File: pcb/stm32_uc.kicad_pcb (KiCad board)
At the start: 2 copper layers, 28 parts, among them J1 Conn_01x18_Male, J2 Conn_01x18_Male, J3 USB_C_Receptacle_USB2.0, J4 Conn_01x04_Male, SW1 SW_SPDT, U1 AMS1117-3.3, U2 STM32F103C8T6, Y1 16Mhz

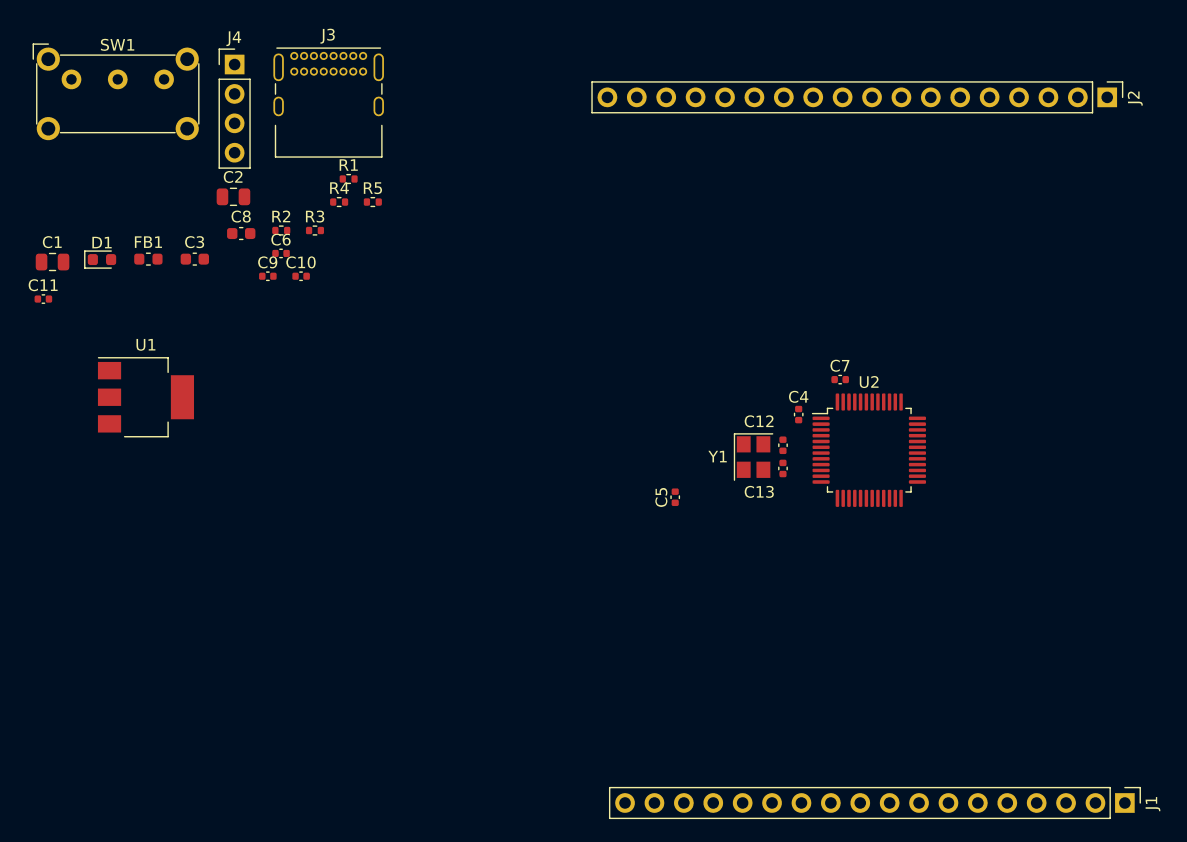
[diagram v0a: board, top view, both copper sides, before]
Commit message: fix pin header pinout
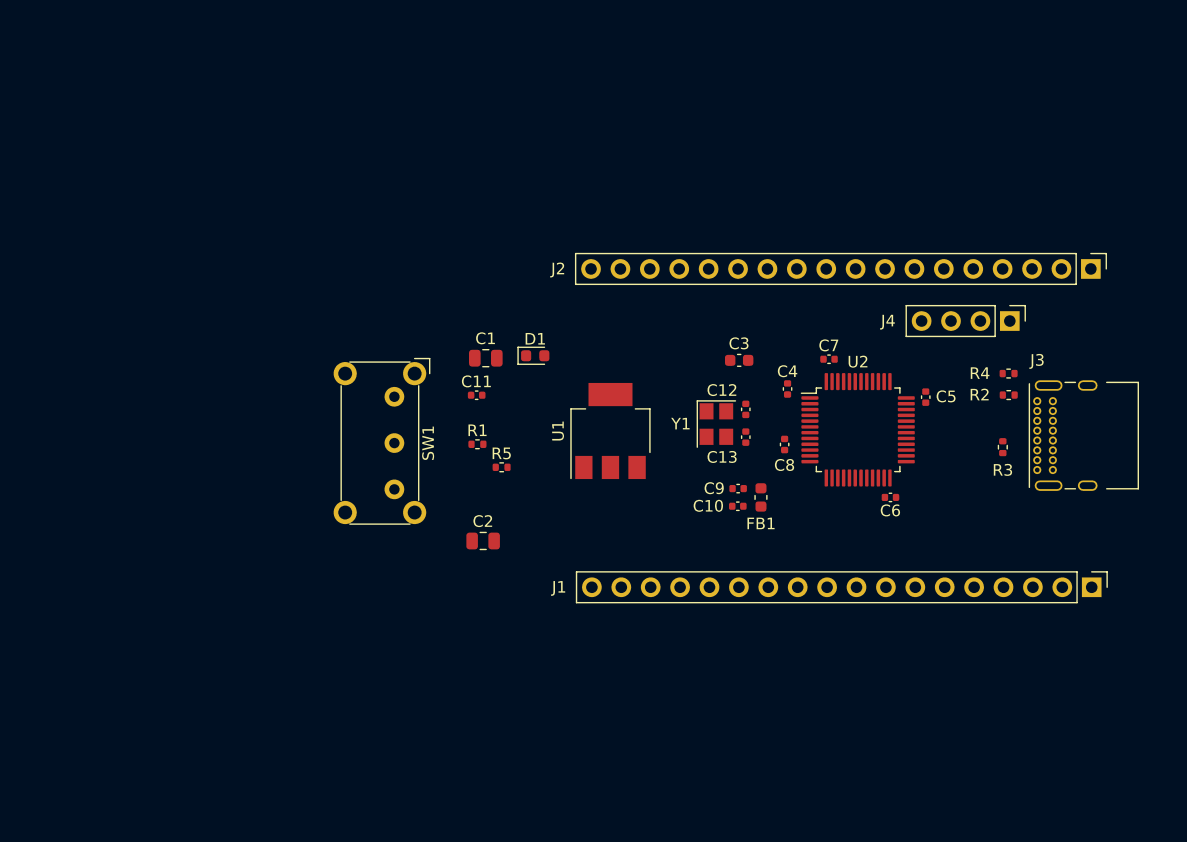
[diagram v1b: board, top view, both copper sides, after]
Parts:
- C8: footprint Capacitor_SMD:C_0603_1608Metric -> Capacitor_SMD:C_0402_1005Metric
- moved J3 73.5 mm to (195.9, 106.9), turned to 90 degrees
- moved J4 70.5 mm to (193.5, 94.0), turned to -90 degrees
- moved R2 64.4 mm to (193.4, 100.4), turned to 180 degrees
- moved R3 62.3 mm to (192.9, 104.9), turned to 90 degrees
- moved R4 59.7 mm to (193.4, 98.5), turned to 180 degrees
- moved FB1 56.8 mm to (172.0, 109.2), turned to -90 degrees
- moved C6 56.7 mm to (183.2, 109.2), turned to 180 degrees
- moved C8 50.4 mm to (174.0, 104.7), turned to 90 degrees
- moved C3 47.8 mm to (170.1, 97.4)
- moved C9 44.6 mm to (170.0, 108.5), turned to 180 degrees
- moved C10 42.6 mm to (170.0, 110.0), turned to 180 degrees
- moved U1 40.2 mm to (159.0, 103.5), turned to 90 degrees
- moved SW1 39.1 mm to (140.3, 100.5), turned to -90 degrees
- moved D1 38.3 mm to (152.5, 97.0)
- moved C11 38.3 mm to (147.4, 100.4)
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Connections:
- J1 pad 10: /PA3 -> /PA7
- J1 pad 11: /PA4 -> /PA6
- J1 pad 13: /PA6 -> /PA4
- J1 pad 14: /PA7 -> /PA3
- J1 pad 15: /PA8 -> /PA2
- J1 pad 16: /PA9 -> /PA1
- J1 pad 17: /PA15 -> /PA0
- J1 pad 2: /PB11 -> /PB14
- J1 pad 3: /PB12 -> /PB13
- J1 pad 4: /PB13 -> /PB12
- J1 pad 5: /PB14 -> /PB11
- J1 pad 6: /PB15 -> /PB10
- J1 pad 7: /PA0 -> /PB2
- J1 pad 8: /PA1 -> /PB1
- J1 pad 9: /PA2 -> /PB0
- J2 pad 10: /PB4 -> /PB7
- J2 pad 11: /PB5 -> /PB8
- J2 pad 12: /PB6 -> /PB9
- J2 pad 13: /PB7 -> unconnected-(J2-Pad13)
- J2 pad 14: /PB8 -> /PC13
- J2 pad 15: /PB9 -> /PC14
- J2 pad 16: /PB10 -> /PC15
- J2 pad 3: /PC13 -> /PB15
- J2 pad 4: /PC14 -> /PA8
- J2 pad 5: /PC15 -> /PA9
- J2 pad 6: /PB0 -> /PB3
- J2 pad 7: /PB1 -> /PB4
- J2 pad 8: /PB2 -> /PB5
- J2 pad 9: /PB3 -> /PB6
- J3 pad A6: Net-(J3-PadA6) -> /USB_D+
- J3 pad A7: Net-(J3-PadA7) -> /USB_D-
- J3 pad B6: Net-(J3-PadA6) -> /USB_D+
- J3 pad B7: Net-(J3-PadA7) -> /USB_D-
- R3 pad 2: Net-(J3-PadA6) -> /USB_D+

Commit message: fix
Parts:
- SW1: footprint Button_Switch_THT:SW_E-Switch_EG1224_SPDT_Angled -> Button_Switch_SMD:SW_SPDT_PCM12
- moved SW1 13.4 mm to (148.0, 89.5), turned to 180 degrees
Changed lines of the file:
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@@
     )
   )
-  (footprint "Button_Switch_THT:SW_E-Switch_EG1224_SPDT_Angled" (layer "F.Cu")
-    (at 140.3325 100.5425 -90)
-    (descr "E-Switch slide switch, EG series, SPDT, right angle, http://spec_sheets.e-switch.com/specs/P040042.pdf")
-    (tags "switch SPDT")
+  (footprint "Button_Switch_SMD:SW_SPDT_PCM12" (layer "F.Cu")
+    (at 148 89.5 180)
+    (descr "Ultraminiature Surface Mount Slide Switch, right-angle, https://www.ckswitches.com/media/1424/pcm.pdf")
     (property "Sheetfile" "stm32_uc.kicad_sch")
     (property "Sheetname" "")
-    (attr through_hole)
-    (fp_text reference "SW1" (at 4 -2.95 90) (layer "F.SilkS")
+    (attr smd)
+    (fp_text reference "SW1" (at 0 -3.2) (layer "F.SilkS")
       (effects (font (size 1 1) (thickness 0.15)))
     )
-    (fp_text value "SW_SPDT" (at 4 14.45 90) (layer "F.Fab")
+    (fp_text value "SW_SPDT" (at 0 4.25) (layer "F.Fab")
       (effects (font (size 1 1) (thickness 0.15)))
     )
-    (fp_text user "${REFERENCE}" (at 4 1.25 90) (layer "F.Fab")
-      (effects (font (size 1 1) (thickness 0.1)))
+    (fp_text user "${REFERENCE}" (at 0 -3.2) (layer "F.Fab")
+      (effects (font (size 1 1) (thickness 0.15)))
     )
-    (fp_line (start 11 -1.35) (end 11 3.85) (layer "F.SilkS") (width 0.12))
-    (fp_line (start -3 3.85) (end -3 -1.35) (layer "F.SilkS") (width 0.12))
-    (fp_line (start -3.3 -3.05) (end -2 -3.05) (layer "F.SilkS") (width 0.12))
-    (fp_line (start -0.95 -2.1) (end 8.95 -2.1) (layer "F.SilkS") (width 0.12))
-    (fp_line (start -3.3 -1.75) (end -3.3 -3.05) (layer "F.SilkS") (width 0.12))
-    (fp_line (start 8.95 4.6) (end -0.95 4.6) (layer "F.SilkS") (width 0.12))
-    (fp_line (start 11.25 5.5) (end 8.75 5.5) (layer "F.CrtYd") (width 0.05))
-    (fp_line (start -0.75 5.5) (end -3.25 5.5) (layer "F.CrtYd") (width 0.05))
-    (fp_line (start -0.75 13.75) (end -0.75 5.5) (layer "F.CrtYd") (width 0.05))
-    (fp_line (start 8.75 13.75) (end -0.75 13.75) (layer "F.CrtYd") (width 0.05))
-    (fp_line (start 11.25 -3) (end 11.25 5.5) (layer "F.CrtYd") (width 0.05))
-    (fp_line (start 8.75 5.5) (end 8.75 13.75) (layer "F.CrtYd") (width 0.05))
-    (fp_line (start -3.25 -3) (end 11.25 -3) (layer "F.CrtYd") (width 0.05))
-    (fp_line (start -3.25 5.5) (end -3.25 -3) (layer "F.CrtYd") (width 0.05))
-    (fp_line (start -2.9 4.5) (end -2.9 -1) (layer "F.Fab") (width 0.1))
-    (fp_line (start -1.9 -2) (end -2.9 -1) (layer "F.Fab") (width 0.1))
-    (fp_line (start 4.5 13.5) (end -0.5 13.5) (layer "F.Fab") (width 0.1))
-    (fp_line (start 10.9 4.5) (end -2.9 4.5) (layer "F.Fab") (width 0.1))
-    (fp_line (start 4.5 4.5) (end 4.5 13.5) (layer "F.Fab") (width 0.1))
-    (fp_line (start -0.5 13.5) (end -0.5 4.5) (layer "F.Fab") (width 0.1))
-    (fp_line (start 10.9 -2) (end 10.9 4.5) (layer "F.Fab") (width 0.1))
-    (fp_line (start -1.9 -2) (end 10.9 -2) (layer "F.Fab") (width 0.1))
-    (pad "" thru_hole circle (at 10 4.25 270) (size 2 2) (drill 1.2) (layers *.Cu *.Mask))
-    (pad "" thru_hole circle (at -2 -1.75 270) (size 2 2) (drill 1.2) (layers *.Cu *.Mask))
-    (pad "" thru_hole circle (at 10 -1.75 270) (size 2 2) (drill 1.2) (layers *.Cu *.Mask))
-    (pad "" thru_hole circle (at -2 4.25 270) (size 2 2) (drill 1.2) (layers *.Cu *.Mask))
-    (pad "1" thru_hole circle (at 0 0 270) (size 1.7 1.7) (drill 0.9) (layers *.Cu *.Mask)
+    (fp_line (start -1.6 -1.12) (end 0.1 -1.12) (layer "F.SilkS") (width 0.12))
+    (fp_line (start 3.45 0.72) (end 3.45 -0.07) (layer "F.SilkS") (width 0.12))
+    (fp_line (start -0.1 3.02) (end -0.3 3.23) (layer "F.SilkS") (width 0.12))
+    (fp_line (start 1.4 -1.12) (end 1.6 -1.12) (layer "F.SilkS") (width 0.12))
+    (fp_line (start -3.45 -0.07) (end -3.45 0.72) (layer "F.SilkS") (width 0.12))
+    (fp_line (start -0.1 3.02) (end -0.1 1.73) (layer "F.SilkS") (width 0.12))
+    (fp_line (start -1.2 3.23) (end -0.3 3.23) (layer "F.SilkS") (width 0.12))
+    (fp_line (start -1.4 3.02) (end -1.2 3.23) (layer "F.SilkS") (width 0.12))
+    (fp_line (start -1.4 1.73) (end -1.4 3.02) (layer "F.SilkS") (width 0.12))
+    (fp_line (start -2.85 1.73) (end 2.85 1.73) (layer "F.SilkS") (width 0.12))
+    (fp_line (start 1.65 3.4) (end -1.65 3.4) (layer "F.CrtYd") (width 0.05))
+    (fp_line (start -1.65 3.4) (end -1.65 2.1) (layer "F.CrtYd") (width 0.05))
+    (fp_line (start -4.4 2.1) (end -4.4 -2.45) (layer "F.CrtYd") (width 0.05))
+    (fp_line (start -1.65 2.1) (end -4.4 2.1) (layer "F.CrtYd") (width 0.05))
+    (fp_line (start 4.4 2.1) (end 1.65 2.1) (layer "F.CrtYd") (width 0.05))
+    (fp_line (start 4.4 -2.45) (end 4.4 2.1) (layer "F.CrtYd") (width 0.05))
+    (fp_line (start -4.4 -2.45) (end 4.4 -2.45) (layer "F.CrtYd") (width 0.05))
+    (fp_line (start 1.65 2.1) (end 1.65 3.4) (layer "F.CrtYd") (width 0.05))
+    (fp_line (start -3.35 -1) (end -3.35 1.6) (layer "F.Fab") (width 0.1))
+    (fp_line (start -1.4 2.95) (end -1.2 3.15) (layer "F.Fab") (width 0.1))
+    (fp_line (start -0.1 2.9) (end -0.1 1.6) (layer "F.Fab") (width 0.1))
+    (fp_line (start -1.2 3.15) (end -0.35 3.15) (layer "F.Fab") (width 0.1))
+    (fp_line (start -0.35 3.15) (end -0.15 2.95) (layer "F.Fab") (width 0.1))
+    (fp_line (start 3.35 -1) (end -3.35 -1) (layer "F.Fab") (width 0.1))
+    (fp_line (start -1.4 1.65) (end -1.4 2.95) (layer "F.Fab") (width 0.1))
+    (fp_line (start -0.15 2.95) (end -0.1 2.9) (layer "F.Fab") (width 0.1))
+    (fp_line (start 3.35 1.6) (end 3.35 -1) (layer "F.Fab") (width 0.1))
+    (fp_line (start -3.35 1.6) (end 3.35 1.6) (layer "F.Fab") (width 0.1))
+    (pad "" smd rect (at -3.65 1.43 180) (size 1 0.8) (layers "F.Cu" "F.Paste" "F.Mask"))
+    (pad "" smd rect (at -3.65 -0.78 180) (size 1 0.8) (layers "F.Cu" "F.Paste" "F.Mask"))
+    (pad "" np_thru_hole circle (at -1.5 0.33 180) (size 0.9 0.9) (drill 0.9) (layers *.Cu *.Mask))
+    (pad "" np_thru_hole circle (at 1.5 0.33 180) (size 0.9 0.9) (drill 0.9) (layers *.Cu *.Mask))
+    (pad "" smd rect (at 3.65 -0.78 180) (size 1 0.8) (layers "F.Cu" "F.Paste" "F.Mask"))
+    (pad "" smd rect (at 3.65 1.43 180) (size 1 0.8) (layers "F.Cu" "F.Paste" "F.Mask"))
+    (pad "1" smd rect (at -2.25 -1.43 180) (size 0.7 1.5) (layers "F.Cu" "F.Paste" "F.Mask")
       (net 2 "GND") (pinfunction "A") (pintype "passive"))
-    (pad "2" thru_hole circle (at 4 0 270) (size 1.7 1.7) (drill 0.9) (layers *.Cu *.Mask)
+    (pad "2" smd rect (at 0.75 -1.43 180) (size 0.7 1.5) (layers "F.Cu" "F.Paste" "F.Mask")
       (net 46 "/SW_BOOT0") (pinfunction "B") (pintype "passive"))
-    (pad "3" thru_hole circle (at 8 0 270) (size 1.7 1.7) (drill 0.9) (layers *.Cu *.Mask)
+    (pad "3" smd rect (at 2.25 -1.43 180) (size 0.7 1.5) (layers "F.Cu" "F.Paste" "F.Mask")
       (net 3 "+3V3") (pinfunction "C") (pintype "passive"))
-    (model "${KICAD6_3DMODEL_DIR}/Button_Switch_THT.3dshapes/SW_E-Switch_EG1224_SPDT_Angled.wrl"
+    (model "${KICAD6_3DMODEL_DIR}/Button_Switch_SMD.3dshapes/SW_SPDT_PCM12.wrl"
       (offset (xyz 0 0 0))
       (scale (xyz 1 1 1))

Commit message: finished rough layout
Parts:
- added H1: MountingHole, MountingHole:MountingHole_2.2mm_M2, F.Cu at (188.0, 117.0)
- added H2: MountingHole, MountingHole:MountingHole_2.2mm_M2, F.Cu at (134.5, 92.0)
- added H3: MountingHole, MountingHole:MountingHole_2.2mm_M2, F.Cu at (134.5, 117.0)
- added H4: MountingHole, MountingHole:MountingHole_2.2mm_M2, F.Cu at (188.0, 92.0)
- moved C1 32.0 mm to (176.2, 112.7), turned to 180 degrees
- moved C2 23.8 mm to (171.1, 107.0), turned to -90 degrees
- moved SW1 20.7 mm to (134.0, 104.8), turned to -90 degrees
- moved C10 19.0 mm to (151.0, 110.7)
- moved C12 19.0 mm to (151.7, 102.3)
- moved C13 19.0 mm to (151.7, 104.7)
- moved C4 19.0 mm to (155.3, 100.6)
- moved C5 19.0 mm to (167.2, 101.3)
- moved C6 19.0 mm to (164.2, 109.9)
- moved C7 19.0 mm to (158.9, 98.0)
- moved C8 19.0 mm to (155.0, 105.4)
- moved C9 19.0 mm to (151.0, 109.2)
- moved FB1 19.0 mm to (153.0, 109.9)
- moved U2 19.0 mm to (161.4, 104.1)
- moved Y1 19.0 mm to (149.2, 103.6)
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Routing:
- added copper zone on B.Cu, net GND
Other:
- board outline added: 59.5 x 31 mm

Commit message: signal routing
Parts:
- moved C2 8.68 mm to (176.5, 113.8), turned to 0 degrees
- moved C1 7.59 mm to (182.0, 107.8), turned to -90 degrees
- moved R3 6.95 mm to (177.1, 101.9), turned to -90 degrees
- moved R4 4.12 mm to (186.5, 98.5)
- moved R2 3.80 mm to (179.8, 104.2)
- moved C6 3.61 mm to (167.8, 109.7)
- moved C12 3.42 mm to (155.1, 102.1)
- moved C13 3.42 mm to (155.1, 104.5)
- moved C3 3.42 mm to (155.6, 98.4)
- moved C5 3.42 mm to (170.6, 101.0)
- moved U2 3.42 mm to (164.8, 103.8)
- moved Y1 3.42 mm to (152.6, 103.3)
- moved C8 3.42 mm to (158.4, 105.1)
- moved C4 3.41 mm to (158.7, 100.7)
- moved C7 3.14 mm to (162.0, 97.8)
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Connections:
- J2 pad 10: /PB7 -> /PB6
- J2 pad 11: /PB8 -> /PB7
- J2 pad 12: /PB9 -> /PB8
- J2 pad 13: unconnected-(J2-Pad13) -> /PB9
- J2 pad 6: /PB3 -> /PA15
- J2 pad 7: /PB4 -> /PB3
- J2 pad 8: /PB5 -> /PB4
- J2 pad 9: /PB6 -> /PB5
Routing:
- net GND: track 0.00 -> 31.0 mm, vias 0 -> 6
- net /PB15: track 0.00 -> 20.1 mm, vias 0 -> 1
- net /USB_D+: track 0.00 -> 18.7 mm
- net /USB_D-: track 0.00 -> 18.1 mm, vias 0 -> 1
- net /PA8: track 0.00 -> 18.0 mm, vias 0 -> 1
- net /PA3: track 0.00 -> 17.2 mm
- net /SWDIO: track 0.00 -> 17.0 mm
- net /PA9: track 0.00 -> 15.8 mm, vias 0 -> 1
- net /PB9: track 0.00 -> 15.4 mm
- net /PA4: track 0.00 -> 15.3 mm
- net +3V3: track 0.00 -> 14.5 mm
- net /PB8: track 0.00 -> 13.5 mm
- net /PA5: track 0.00 -> 13.4 mm
- net /SWCLK: track 0.00 -> 13.1 mm
- net /PB7: track 0.00 -> 11.7 mm
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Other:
- board size 59.5 x 31 mm -> 59 x 31 mm
